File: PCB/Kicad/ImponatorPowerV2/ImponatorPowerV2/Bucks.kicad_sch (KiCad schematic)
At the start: 18 parts, among them Q1 AO3400A, Q2 AO3400A, U11 ACS37041, U3 TPS62A01DRLR, U7 TPS62A01DRLR, U8 ACS37041

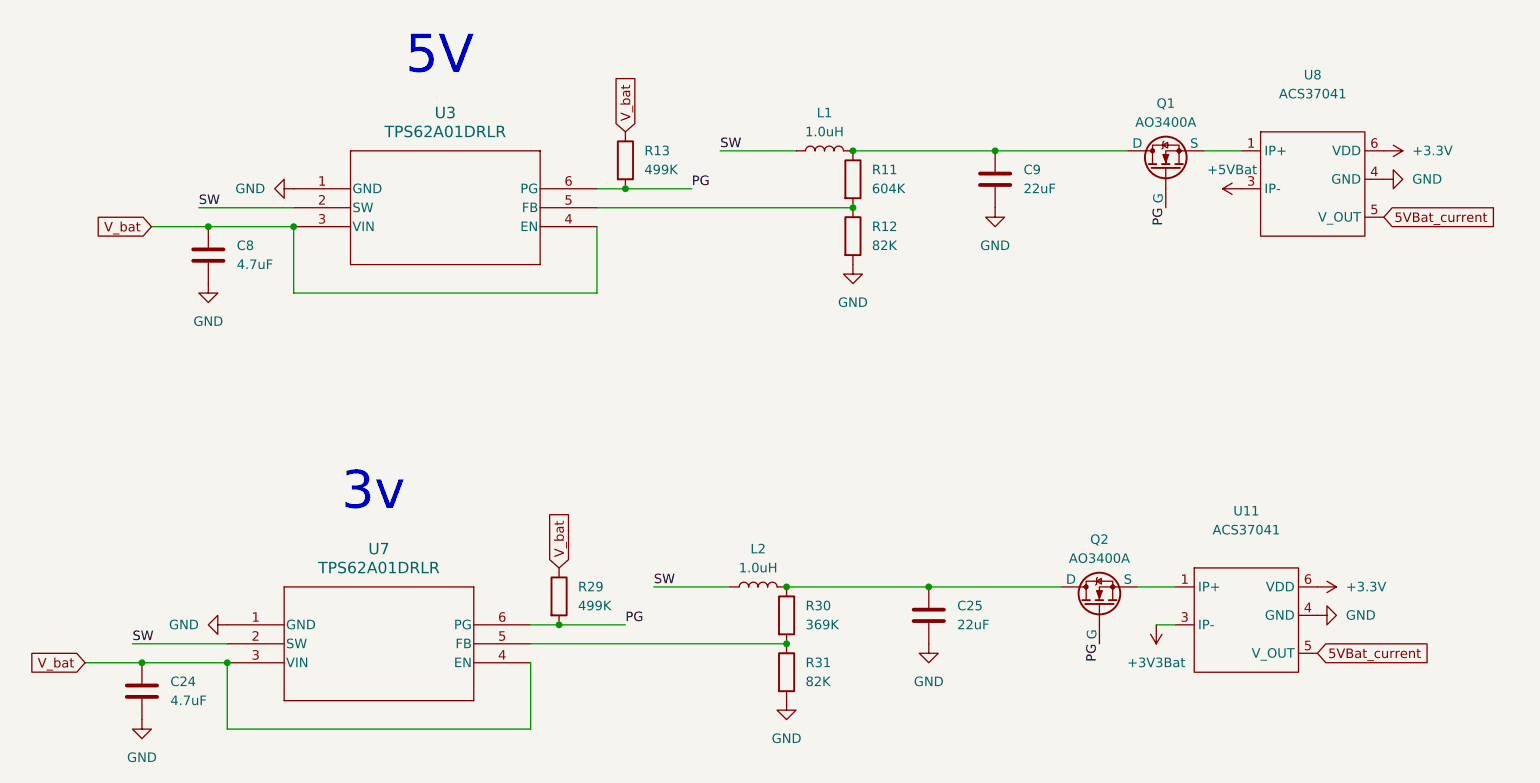
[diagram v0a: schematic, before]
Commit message: PCB routed, not ready for production
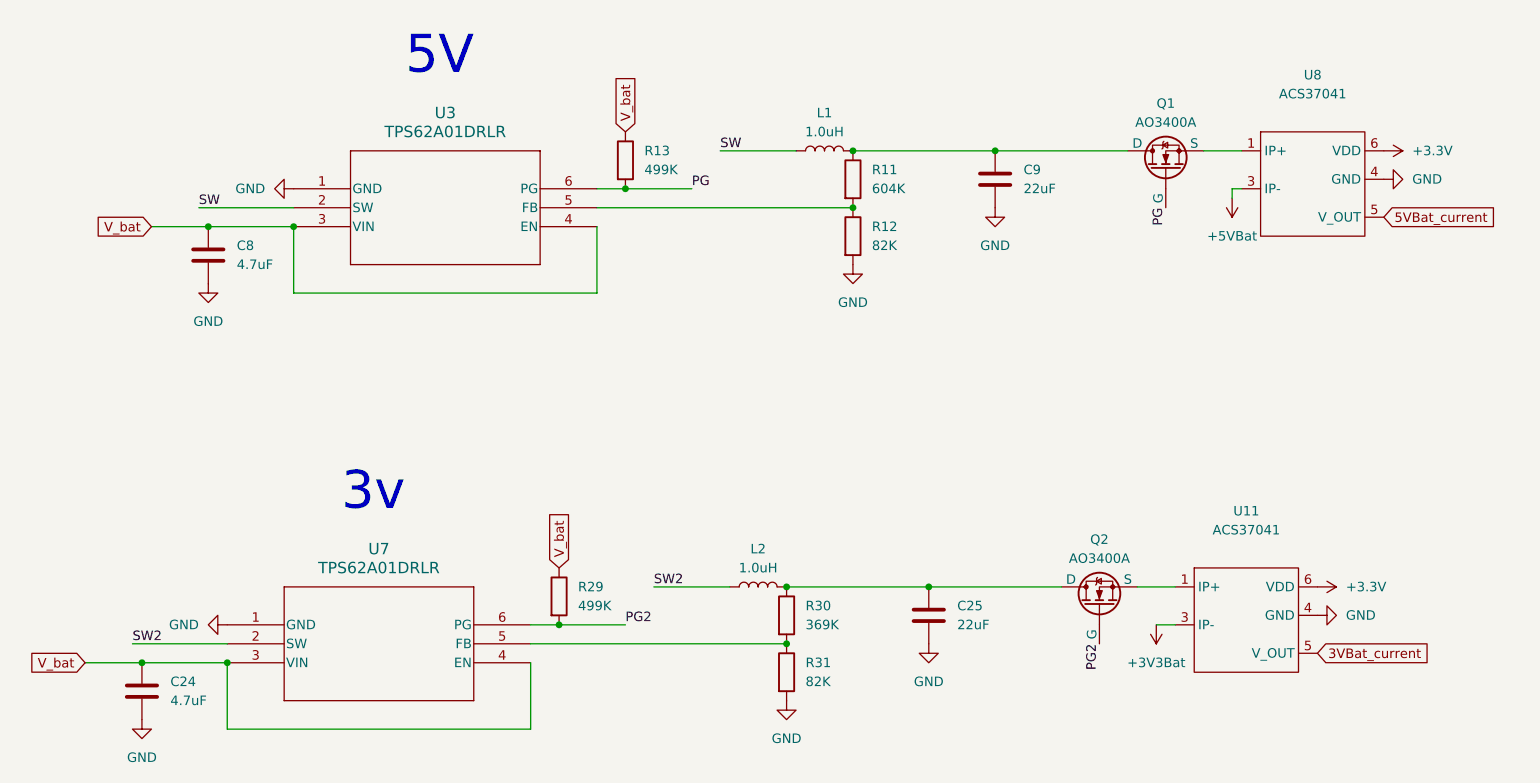
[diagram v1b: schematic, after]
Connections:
- net 5VBat_current: no longer U11.5 (V_OUT)
- net PG: no longer Q2.2 (G), R29.2, U7.6 (PG)
- net SW: no longer L2.1, U7.2 (SW)
- new net 3VBat_current: U11.5 (V_OUT)
- new net PG2: Q2.2 (G), R29.2, U7.6 (PG)
- new net SW2: L2.1, U7.2 (SW)
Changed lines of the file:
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@@
+	(wire
+		(pts
+			(xy 217.17 63.5) (xy 218.44 63.5)
+		)
+		(stroke
+			(width 0)
+			(type default)
+		)
+	)
 	(wire
 		(pts
@@
 		)
 	)
-	(label "PG"
+	(wire
+		(pts
+			(xy 217.17 64.77) (xy 217.17 63.5)
+		)
+		(stroke
+			(width 0)
+			(type default)
+		)
+	)
+	(label "PG2"
 		(at 199.39 124.46 270)
 		(effects
@@
 		)
 	)
-	(label "SW"
+	(label "SW2"
 		(at 69.85 124.46 0)
 		(effects
@@
 		)
 	)
-	(label "PG"
+	(label "PG2"
 		(at 135.89 121.92 0)
 		(effects
@@
 		)
 	)
-	(label "SW"
+	(label "SW2"
 		(at 139.7 116.84 0)
 		(effects
@@
 		)
 	)
-	(global_label "5VBat_current"
+	(global_label "3VBat_current"
 		(shape input)
 		(at 228.6 125.73 0)
@@
 	(symbol
 		(lib_id "power:+5VD")
-		(at 218.44 63.5 90)
+		(at 217.17 64.77 180)
 		(unit 1)
 		(exclude_from_sim no)
@@
 		(fields_autoplaced yes)
 		(property "Reference" "#PWR043567"
-			(at 222.25 63.5 0)
+			(at 217.17 60.96 0)
 			(effects
 				(font
@@
 		)
 		(property "Value" "+5VBat"
-			(at 217.17 60.96 90)
+			(at 217.17 69.85 0)
 			(effects
 				(font
@@
 		)
 		(property "Footprint" ""
-			(at 218.44 63.5 0)
+			(at 217.17 64.77 0)
 			(effects
 				(font
@@
 		)
 		(property "Datasheet" ""
-			(at 218.44 63.5 0)
+			(at 217.17 64.77 0)
 			(effects
 				(font
@@
 		)
 		(property "Description" "Power symbol creates a global label with name \"+5VBat\""
-			(at 218.44 63.5 0)
-			(effects
-				(font
+			(at 217.17 64.77 0)
+			(effects
+				(font
